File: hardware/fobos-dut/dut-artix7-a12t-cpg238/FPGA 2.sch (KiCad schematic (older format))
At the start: 2 parts

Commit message: Started to rewire the CPG238 into the schematic Split FPGA Power and Programming into two sheets since new FPGA symbol explicitly displays each power pin and is much larger
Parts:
- U1: renamed from U?; footprint (none) -> Package_BGA:Xilinx_CPG238
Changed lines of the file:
@@
 $Descr A4 11693 8268
 encoding utf-8
-Sheet 6 7
+Sheet 6 8
 Title ""
 Date ""
@@
 P 8200 1200
 AR Path="/5F22D594/60BFCB35" Ref="U?"  Part="3"
-AR Path="/6004C151/60BFCB35" Ref="U?"  Part="3"
-F 0 "U?" H 10430 -1097 50  0000 L CNN
+AR Path="/6004C151/60BFCB35" Ref="U1"  Part="3"
+F 0 "U1" H 10430 -1097 50  0000 L CNN
 F 1 "XC7A12T-CPG238" H 10430 -1188 50  0000 L CNN
-F 2 "" H 8200 1200 50  0001 C CNN
+F 2 "Package_BGA:Xilinx_CPG238" H 8200 1200 50  0001 C CNN
 F 3 "" H 8200 1200 50  0001 C CNN
 	3    8200 1200
@@
 $EndComp
 $Comp
-L cerg:XC7A12T-CPG238 U?
+L cerg:XC7A12T-CPG238 U1
 U 5 1 60C0A0EC
 P 2500 2350
-F 0 "U?" H 4730 53  50  0000 L CNN
+F 0 "U1" H 4730 53  50  0000 L CNN
 F 1 "XC7A12T-CPG238" H 4730 -38 50  0000 L CNN
-F 2 "" H 2500 2350 50  0001 C CNN
+F 2 "Package_BGA:Xilinx_CPG238" H 2500 2350 50  0001 C CNN
 F 3 "" H 2500 2350 50  0001 C CNN
 	5    2500 2350

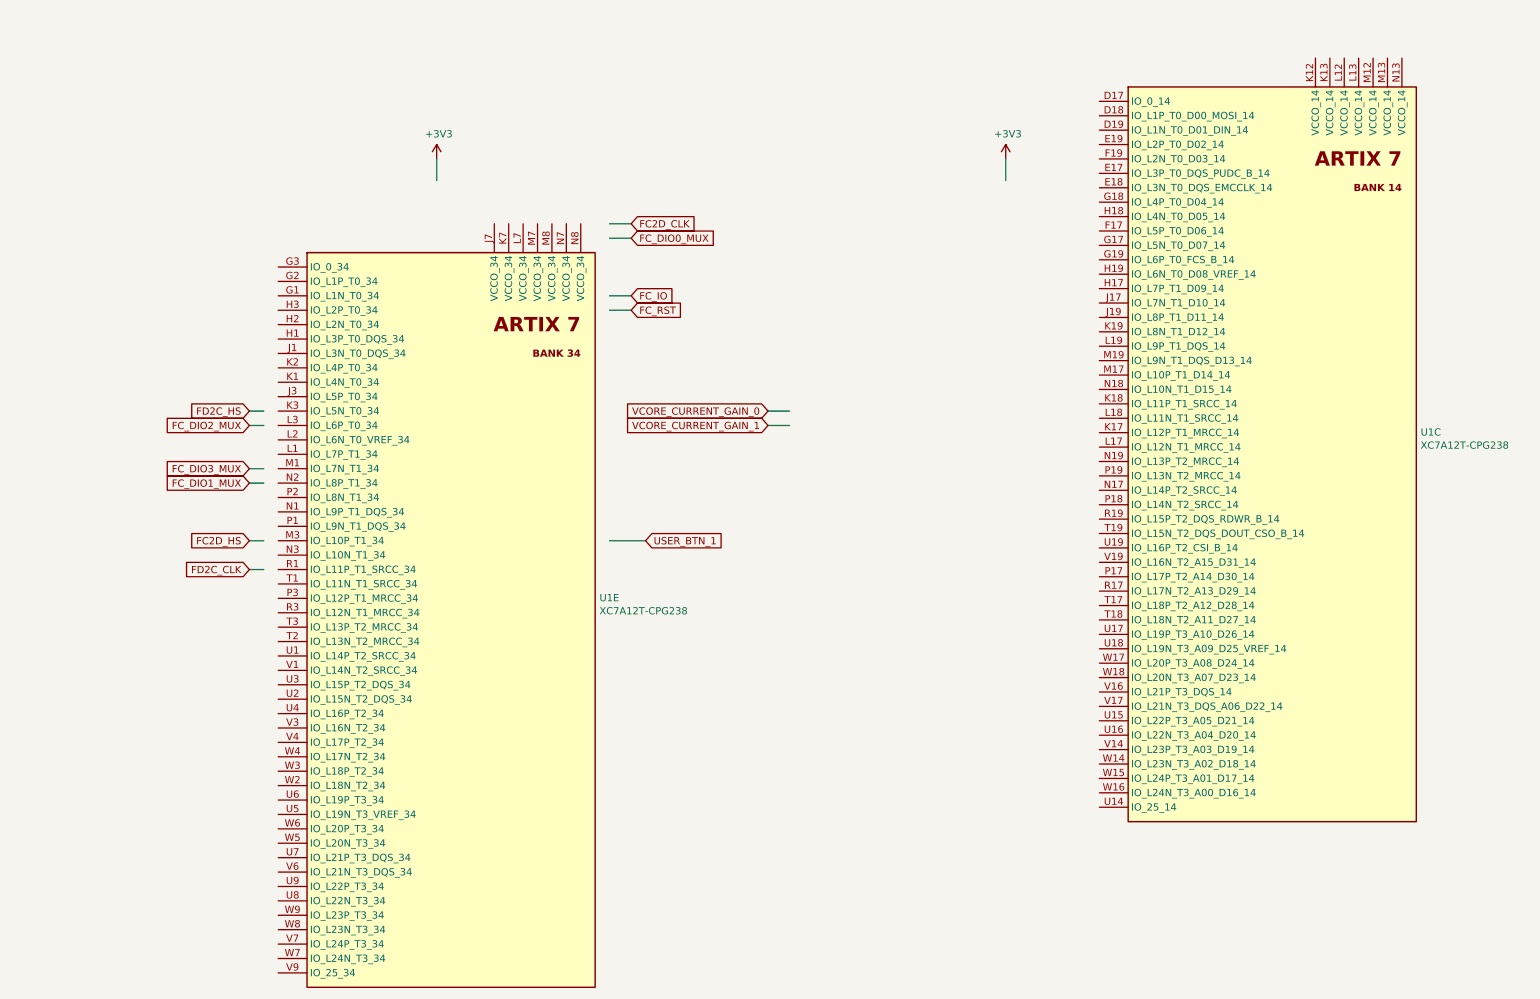
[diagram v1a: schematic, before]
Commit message: Connected the fixed signals to the FPGA, flexible IO are left unconnected Added 0.1 ohm resistors to the 1V8 and 3V3 power rails, added test points which allow for easy measurement Updated ARTIX7-A12T-CPG238 symbol to make schematic route similarly to the last symbol Connected CFGVBS signal to the 3V3 rail, was previously connected to VCCINT which was a mistake Ran through 7 Series schematic review checklist - 7_Series_Schematic_Review_Recommendations.xlsm Added Xilinx pinout files for the CPG238 package Generated schematic for the csg325 for easy referencing
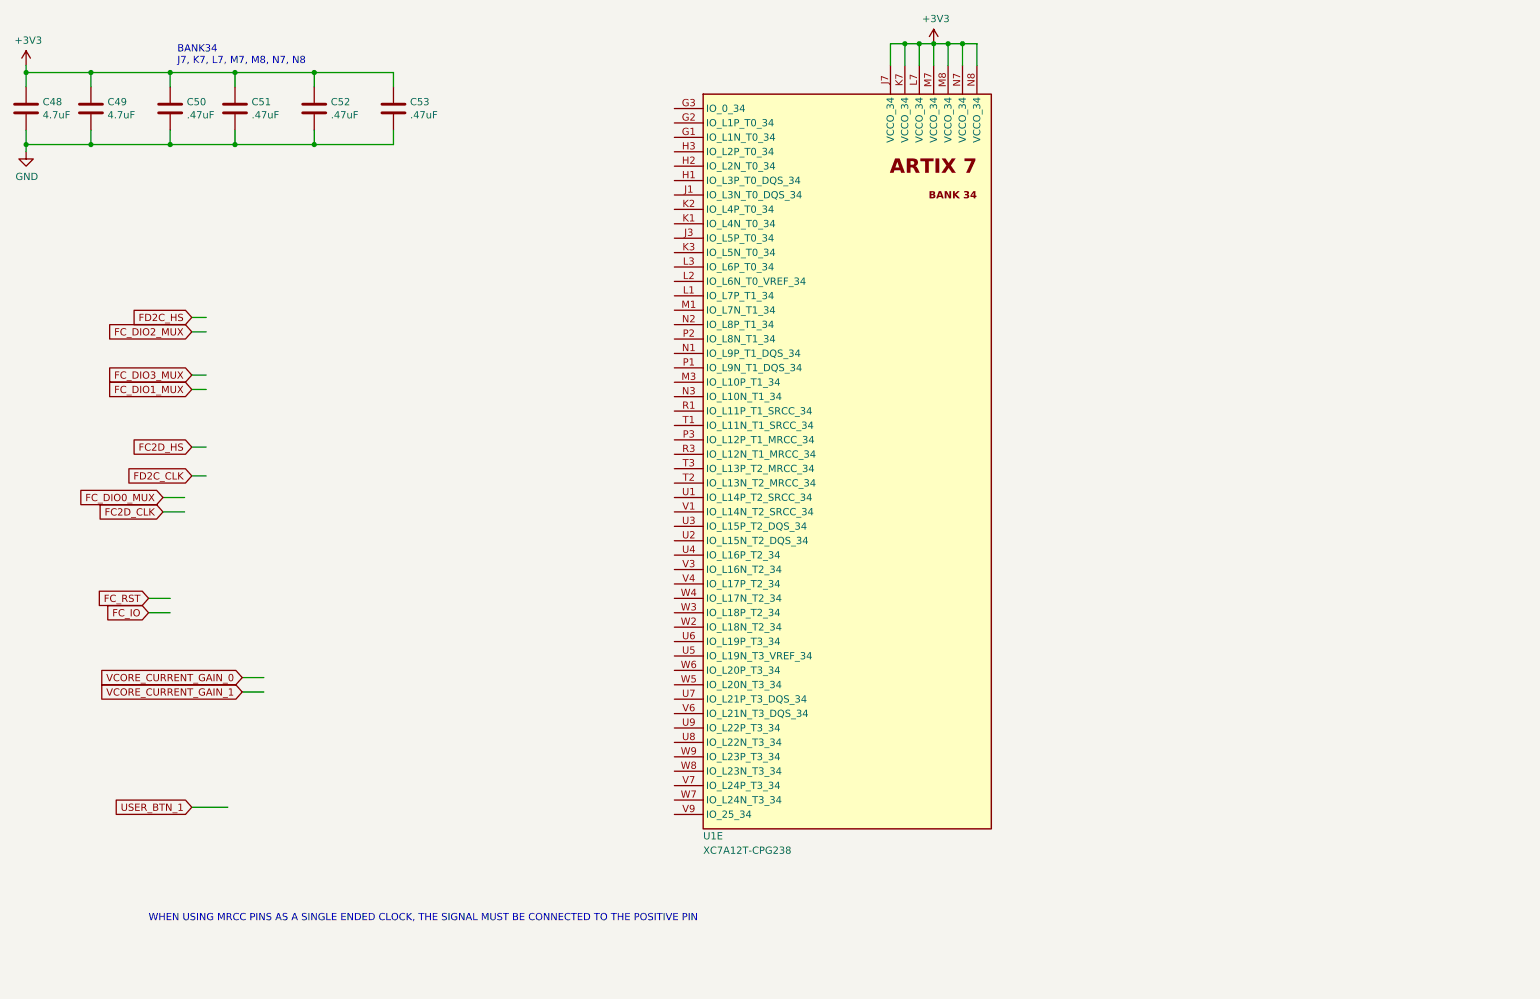
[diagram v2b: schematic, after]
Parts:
- removed unit 3 of U1
- added C48, C49: 4.7uF, Capacitor_SMD:C_0402_1005Metric_Pad0.74x0.62mm_HandSolder, symbol Device:C
- added C50, C51, C52, C53: .47uF, Capacitor_SMD:C_0402_1005Metric_Pad0.74x0.62mm_HandSolder, symbol Device:C
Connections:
- net labels added: GND
- wire segments 15 -> 50
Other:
- note added: "BANK34\nJ7, K7, L7, M7, M8, N7, N8"
- note added: "WHEN USING MRCC PINS AS A SINGLE ENDED CLOCK, THE SIGNAL MUST BE CONNECTED TO THE POSITIVE PIN"
- moved on the sheet: U1E

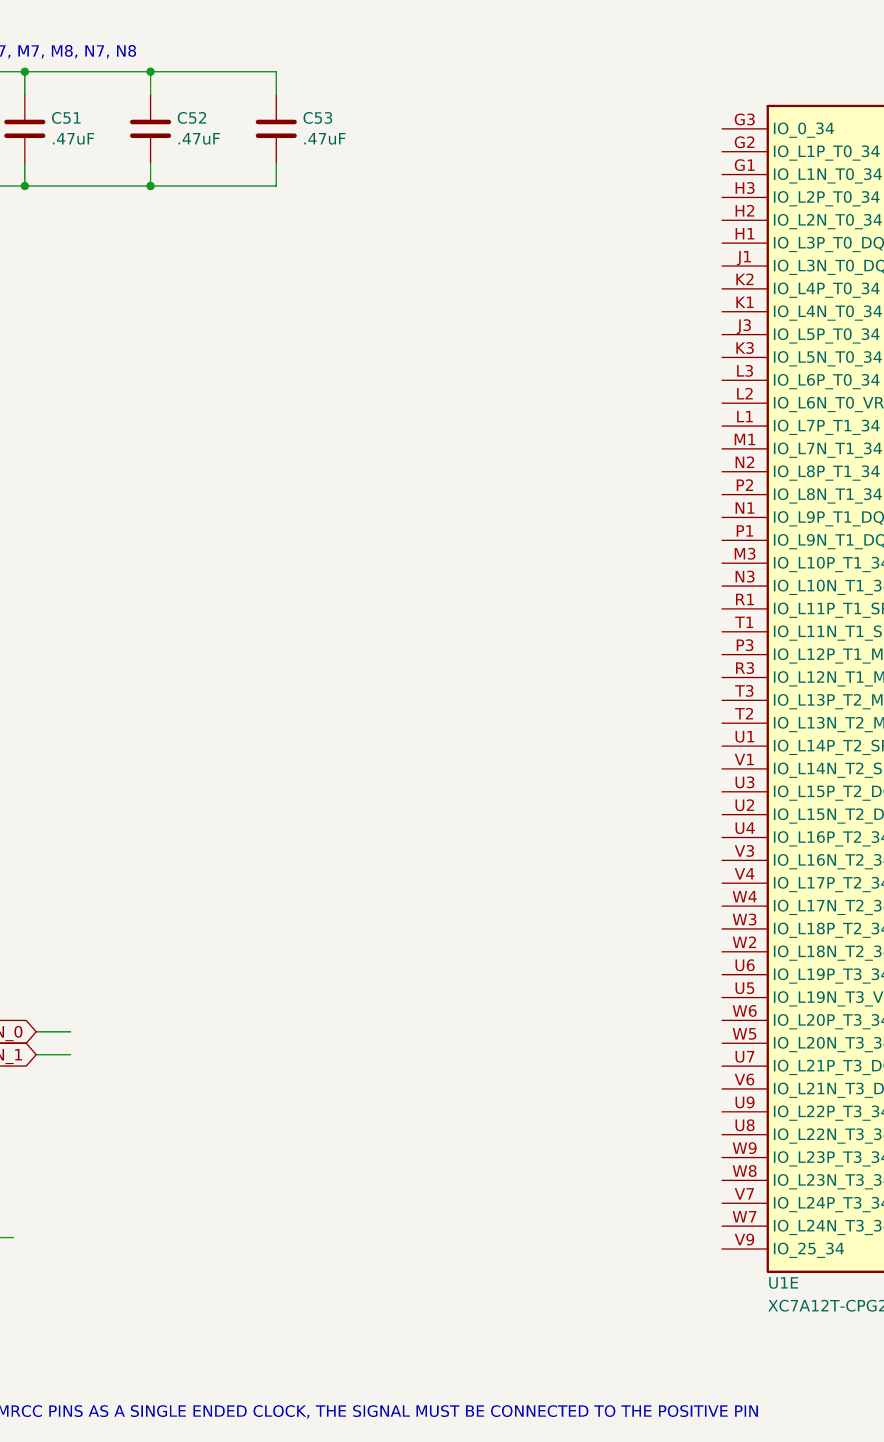
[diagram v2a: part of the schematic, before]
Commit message: Updated escape routing of most pads to take advantage of "pad sacrifices"
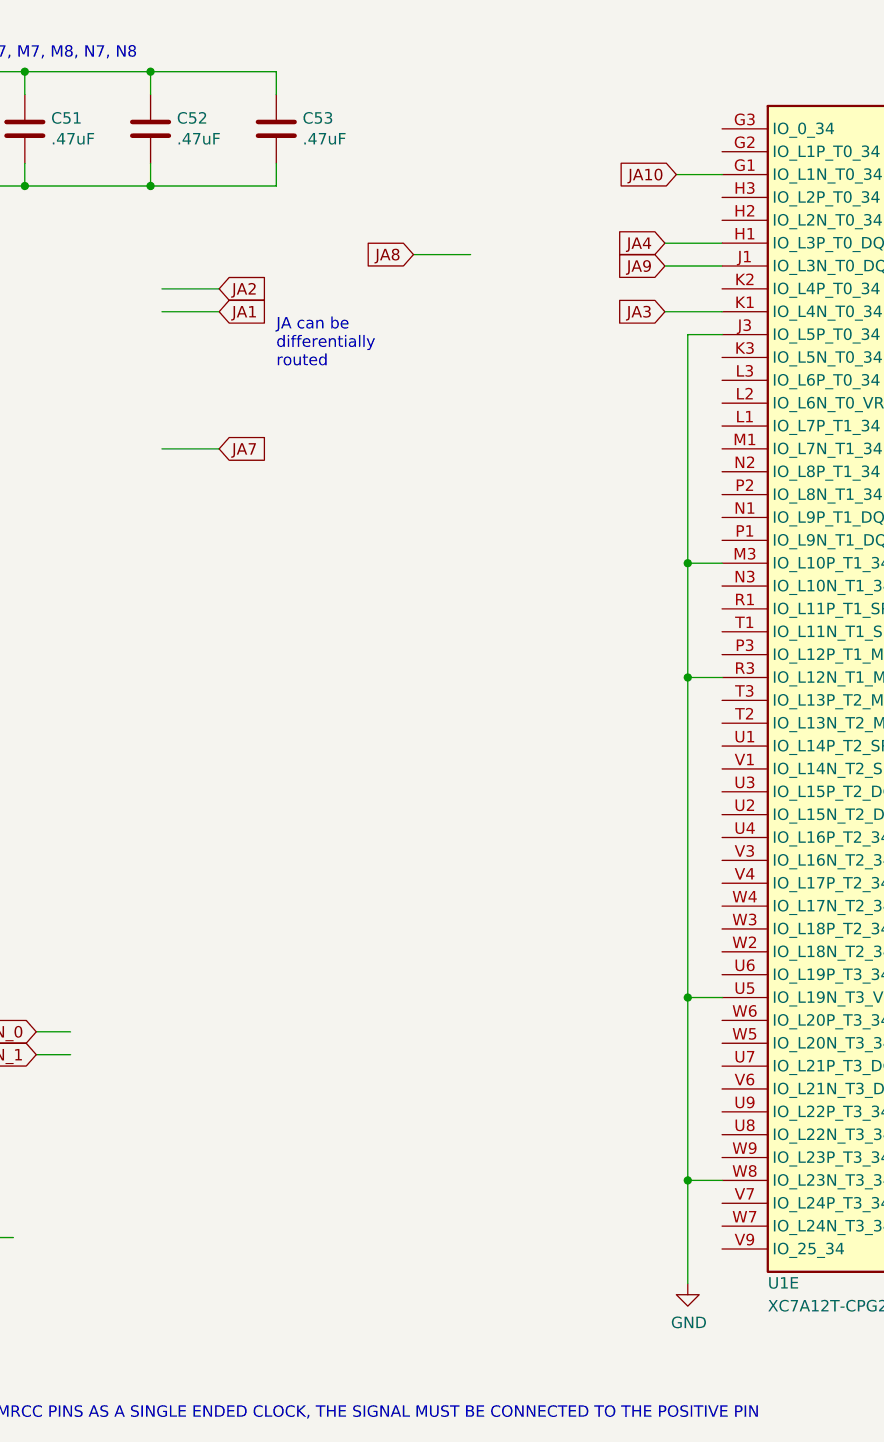
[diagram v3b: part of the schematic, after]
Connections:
- net labels added: JA1, JA10, JA2, JA3, JA4, JA7, JA8, JA9
- wire segments 50 -> 68
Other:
- note added: "JA can be \ndifferentially\nrouted"
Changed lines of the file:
@@
 Text Notes 1600 6900 0    50   ~ 0
 WHEN USING MRCC PINS AS A SINGLE ENDED CLOCK, THE SIGNAL MUST BE CONNECTED TO THE POSITIVE PIN
+Text GLabel 3050 2050 2    50   Input ~ 0
+JA1
+Text GLabel 3050 2650 2    50   Input ~ 0
+JA7
+Text GLabel 3050 1950 2    50   Input ~ 0
+JA2
+Text GLabel 3900 1800 0    50   Input ~ 0
+JA8
+Text GLabel 5000 2050 0    50   Input ~ 0
+JA3
+Text GLabel 5000 1850 0    50   Input ~ 0
+JA9
+Text GLabel 5000 1750 0    50   Input ~ 0
+JA4
+Wire Wire Line
+	3050 2050 2800 2050
+Wire Wire Line
+	2800 2650 3050 2650
+Wire Wire Line
+	2800 1950 3050 1950
+Wire Wire Line
+	3900 1800 4150 1800
+Wire Wire Line
+	5000 2050 5250 2050
+Wire Wire Line
+	5000 1850 5250 1850
+Wire Wire Line
+	5000 1750 5250 1750
+Text Notes 3300 2300 0    50   ~ 0
+JA can be \ndifferentially\nrouted
+Text GLabel 5050 1450 0    50   Input ~ 0
+JA10
+Wire Wire Line
+	5050 1450 5250 1450
+$Comp
+L power:GND #PWR?
+U 1 1 61EBD061
+P 5100 6300
+AR Path="/5F3A1954/61EBD061" Ref="#PWR?"  Part="1"
+AR Path="/60D2F94F/61EBD061" Ref="#PWR?"  Part="1"
+AR Path="/6004C151/61EBD061" Ref="#PWR0135"  Part="1"
+F 0 "#PWR0135" H 5100 6050 50  0001 C CNN
+F 1 "GND" H 5105 6127 50  0000 C CNN
+F 2 "" H 5100 6300 50  0001 C CNN
+F 3 "" H 5100 6300 50  0001 C CNN
+	1    5100 6300
+	1    0    0    -1
+$EndComp
+Wire Wire Line
+	5250 2150 5100 2150
+Wire Wire Line
+	5100 2150 5100 3150
+Wire Wire Line
+	5250 3150 5100 3150
+Connection ~ 5100 3150
+Wire Wire Line
+	5100 3150 5100 3650
+Wire Wire Line
+	5250 3650 5100 3650
+Connection ~ 5100 3650
+Wire Wire Line
+	5100 3650 5100 5050
+Wire Wire Line
+	5250 5050 5100 5050
+Connection ~ 5100 5050
+Wire Wire Line
+	5100 5050 5100 5850
+Wire Wire Line
+	5250 5850 5100 5850
+Connection ~ 5100 5850
+Wire Wire Line
+	5100 5850 5100 6300
 $EndSCHEMATC
